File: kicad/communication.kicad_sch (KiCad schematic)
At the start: 24 parts, among them J1 Screw_Terminal_01x03, J2 Screw_Terminal_01x03, J3 Conn_ARM_SWD_TagConnect_TC203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, P1 GT-USB-7014F

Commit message: [simulations] Added debouncing, added RC circuit, cleaned up LC-ladder, [scripts] (filtering) added usb-section, started working on debouncing equations, [kicad] Additional CAN configuration added, filtering capacitor added for USB-power section
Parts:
- added C30: 1uF, symbol Device:C_Small
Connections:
- net GND: now also C30.2
- net USB_VBUS: now also C30.1
- no-connect marks 12 -> 13
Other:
- note added: "Add 1 uF capacitor for filtering (pole: 1/(1e-6) > 1 MHz)"
- note added: "TXD, NSIL, STBY internally pulled-up STBY: pulled down to enable normal-mode"
- moved on the sheet: R36
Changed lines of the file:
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@@
   (junction (at 172.72 30.48) (diameter 0) (color 0 0 0 0)
   )
+  (junction (at 58.42 173.355) (diameter 0) (color 0 0 0 0)
+  )
   (junction (at 152.4 46.99) (diameter 0) (color 0 0 0 0)
   )
@@
   )
   (junction (at 168.91 30.48) (diameter 0) (color 0 0 0 0)
-  )
-  (junction (at 58.42 170.18) (diameter 0) (color 0 0 0 0)
   )
   (junction (at 72.39 54.61) (diameter 0) (color 0 0 0 0)
@@
   (no_connect (at 91.44 109.22))
   (no_connect (at 91.44 124.46))
+  (no_connect (at 53.34 48.26))
   (no_connect (at 91.44 127))
   (no_connect (at 91.44 132.08))
@@
   (no_connect (at 91.44 104.14))
   (no_connect (at 91.44 134.62))
+  (wire (pts (xy 48.895 44.45) (xy 53.34 44.45))
+    (stroke (width 0) (type default))
+  )
   (wire (pts (xy 163.83 77.47) (xy 163.83 86.36))
     (stroke (width 0) (type default))
@@
     (stroke (width 0) (type default))
   )
+  (wire (pts (xy 43.18 166.37) (xy 43.18 165.1))
+    (stroke (width 0) (type default))
+  )
   (wire (pts (xy 168.91 41.91) (xy 176.53 41.91))
     (stroke (width 0) (type default))
@@
     (stroke (width 0) (type default))
   )
+  (wire (pts (xy 58.42 174.625) (xy 58.42 173.355))
+    (stroke (width 0) (type default))
+  )
   (wire (pts (xy 91.44 160.02) (xy 58.42 160.02))
     (stroke (width 0) (type default))
   )
-  (wire (pts (xy 52.07 170.18) (xy 58.42 170.18))
+  (wire (pts (xy 55.245 173.355) (xy 58.42 173.355))
     (stroke (width 0) (type default))
   )
@@
     (stroke (width 0) (type default))
   )
+  (wire (pts (xy 58.42 167.64) (xy 58.42 173.355))
+    (stroke (width 0) (type default))
+  )
   (wire (pts (xy 172.72 38.1) (xy 172.72 39.37))
     (stroke (width 0) (type default))
@@
     (stroke (width 0) (type default))
   )
+  (wire (pts (xy 58.42 180.34) (xy 58.42 179.705))
+    (stroke (width 0) (type default))
+  )
   (wire (pts (xy 72.39 49.53) (xy 77.47 49.53))
     (stroke (width 0) (type default))
@@
     (stroke (width 0) (type default))
   )
-  (wire (pts (xy 58.42 177.8) (xy 58.42 179.07))
-    (stroke (width 0) (type default))
-  )
   (wire (pts (xy 72.39 54.61) (xy 72.39 49.53))
     (stroke (width 0) (type default))
@@
     (stroke (width 0) (type default))
   )
-  (wire (pts (xy 58.42 167.64) (xy 58.42 170.18))
-    (stroke (width 0) (type default))
-  )
   (wire (pts (xy 93.98 46.99) (xy 90.17 46.99))
     (stroke (width 0) (type default))
@@
     (stroke (width 0) (type default))
   )
-  (wire (pts (xy 58.42 170.18) (xy 58.42 172.72))
-    (stroke (width 0) (type default))
-  )
   (wire (pts (xy 106.68 93.98) (xy 114.3 93.98))
     (stroke (width 0) (type default))
@@
   )
   (wire (pts (xy 157.48 83.82) (xy 168.91 83.82))
+    (stroke (width 0) (type default))
+  )
+  (wire (pts (xy 43.18 161.29) (xy 43.18 160.02))
     (stroke (width 0) (type default))
   )
@@
     (effects (font (size 1.27 1.27)) (justify left bottom))
   )
+  (text "Add 1 uF capacitor for filtering (pole: 1/(1e-6) > 1 MHz)"
+    (at 43.18 194.945 0)
+    (effects (font (size 1.27 1.27)) (justify left bottom))
+  )
+  (text "TXD, NSIL, STBY internally pulled-up\nSTBY: pulled down to enable normal-mode"
+    (at 27.94 78.105 0)
+    (effects (font (size 1.27 1.27)) (justify left bottom))
+  )
   (text "Pull-up resistors chosen at random\nwon't work for high bus-capacitance + speed"
     (at 138.43 95.25 0)
@@
     )
   )
-  (global_label "USB_SENSE" (shape input) (at 52.07 170.18 180) (fields_autoplaced)
+  (global_label "USB_SENSE" (shape input) (at 55.245 173.355 180) (fields_autoplaced)
     (effects (font (size 1.27 1.27)) (justify right))
-    (property "Intersheetrefs" "${INTERSHEET_REFS}" (at 38.2597 170.18 0)
+    (property "Intersheetrefs" "${INTERSHEET_REFS}" (at 41.4347 173.355 0)
       (effects (font (size 1.27 1.27)) (justify right) hide)
     )
@@
     )
   )
-  (symbol (lib_id "power:GND") (at 58.42 179.07 0) (unit 1)
-    (in_bom yes) (on_board yes) (dnp no) (fields_autoplaced)
-    (property "Reference" "#PWR031" (at 58.42 185.42 0)
-      (effects (font (size 1.27 1.27)) hide)
-    )
-    (property "Value" "GND" (at 58.42 184.15 0)
-      (effects (font (size 1.27 1.27)))
-    )
-    (property "Footprint" "" (at 58.42 179.07 0)
-      (effects (font (size 1.27 1.27)) hide)
-    )
-    (property "Datasheet" "" (at 58.42 179.07 0)
+  (symbol (lib_id "power:GND") (at 58.42 180.34 0) (unit 1)
+    (in_bom yes) (on_board yes) (dnp no) (fields_autoplaced)
+    (property "Reference" "#PWR031" (at 58.42 186.69 0)
+      (effects (font (size 1.27 1.27)) hide)
+    )
+    (property "Value" "GND" (at 58.42 185.42 0)
+      (effects (font (size 1.27 1.27)))
+    )
+    (property "Footprint" "" (at 58.42 180.34 0)
+      (effects (font (size 1.27 1.27)) hide)
+    )
+    (property "Datasheet" "" (at 58.42 180.34 0)
       (effects (font (size 1.27 1.27)) hide)
     )
@@
     )
   )
-  (symbol (lib_id "Device:R_Small") (at 58.42 175.26 0) (unit 1)
-    (in_bom yes) (on_board yes) (dnp no) (fields_autoplaced)
-    (property "Reference" "R36" (at 60.96 173.99 0)
-      (effects (font (size 1.27 1.27)) (justify left))
-    )
-    (property "Value" "21k" (at 60.96 176.53 0)
-      (effects (font (size 1.27 1.27)) (justify left))
-    )
-    (property "Footprint" "" (at 58.42 175.26 0)
-      (effects (font (size 1.27 1.27)) hide)
-    )
-    (property "Datasheet" "~" (at 58.42 175.26 0)
+  (symbol (lib_id "Device:R_Small") (at 58.42 177.165 0) (unit 1)
+    (in_bom yes) (on_board yes) (dnp no) (fields_autoplaced)
+    (property "Reference" "R36" (at 60.96 175.895 0)
+      (effects (font (size 1.27 1.27)) (justify left))
+    )
+    (property "Value" "21k" (at 60.96 178.435 0)
+      (effects (font (size 1.27 1.27)) (justify left))
+    )
+    (property "Footprint" "" (at 58.42 177.165 0)
+      (effects (font (size 1.27 1.27)) hide)
+    )
+    (property "Datasheet" "~" (at 58.42 177.165 0)
       (effects (font (size 1.27 1.27)) hide)
     )
@@
         (path "/91e2f46a-700b-4d7a-a06a-22469f63223f/53dc30ee-9af6-4771-8676-c78726df5d90"
           (reference "R36") (unit 1)
+        )
+      )
+    )
+  )
+  (symbol (lib_id "power:GND") (at 48.895 44.45 0) (unit 1)
+    (in_bom yes) (on_board yes) (dnp no) (fields_autoplaced)
+    (property "Reference" "#PWR059" (at 48.895 50.8 0)
+      (effects (font (size 1.27 1.27)) hide)
+    )
+    (property "Value" "GND" (at 48.895 49.53 0)
+      (effects (font (size 1.27 1.27)))
+    )
+    (property "Footprint" "" (at 48.895 44.45 0)
+      (effects (font (size 1.27 1.27)) hide)
+    )
+    (property "Datasheet" "" (at 48.895 44.45 0)
+      (effects (font (size 1.27 1.27)) hide)
+    )
+    (pin "1")
+    (instances
+      (project "bldc_project"
+        (path "/91e2f46a-700b-4d7a-a06a-22469f63223f/53dc30ee-9af6-4771-8676-c78726df5d90"
+          (reference "#PWR059") (unit 1)
         )
       )
@@
     )
   )
+  (symbol (lib_id "Device:C_Small") (at 43.18 163.83 0) (unit 1)
+    (in_bom yes) (on_board yes) (dnp no) (fields_autoplaced)
+    (property "Reference" "C30" (at 45.72 162.5663 0)
+      (effects (font (size 1.27 1.27)) (justify left))
+    )
+    (property "Value" "1uF" (at 45.72 165.1063 0)
+      (effects (font (size 1.27 1.27)) (justify left))
+    )
+    (property "Footprint" "" (at 43.18 163.83 0)
+      (effects (font (size 1.27 1.27)) hide)
+    )
+    (property "Datasheet" "~" (at 43.18 163.83 0)
+      (effects (font (size 1.27 1.27)) hide)
+    )
+    (pin "2")
+    (pin "1")
+    (instances
+      (project "bldc_project"
+        (path "/91e2f46a-700b-4d7a-a06a-22469f63223f/53dc30ee-9af6-4771-8676-c78726df5d90"
+          (reference "C30") (unit 1)
+        )
+      )
+    )
+  )
   (symbol (lib_id "Diode:SMAJ13A") (at 172.72 34.29 90) (unit 1)
     (in_bom yes) (on_board yes) (dnp no)
@@
         )
       )
+    )
+  )
+  (symbol (lib_id "power:GND") (at 43.18 165.1 0) (unit 1)
+    (in_bom yes) (on_board yes) (dnp no) (fields_autoplaced)
+    (property "Reference" "#PWR058" (at 43.18 171.45 0)
+      (effects (font (size 1.27 1.27)) hide)
+    )
+    (property "Value" "GND" (at 43.18 170.18 0)
+      (effects (font (size 1.27 1.27)))
+    )
+    (property "Footprint" "" (at 43.18 165.1 0)
+      (effects (font (size 1.27 1.27)) hide)
+    )
+    (property "Datasheet" "" (at 43.18 165.1 0)
+      (effects (font (size 1.27 1.27)) hide)
+    )
+    (pin "1")
+    (instances
+      (project "bldc_project"
+        (path "/91e2f46a-700b-4d7a-a06a-22469f63223f/53dc30ee-9af6-4771-8676-c78726df5d90"
+          (reference "#PWR058") (unit 1)
+        )
+      )

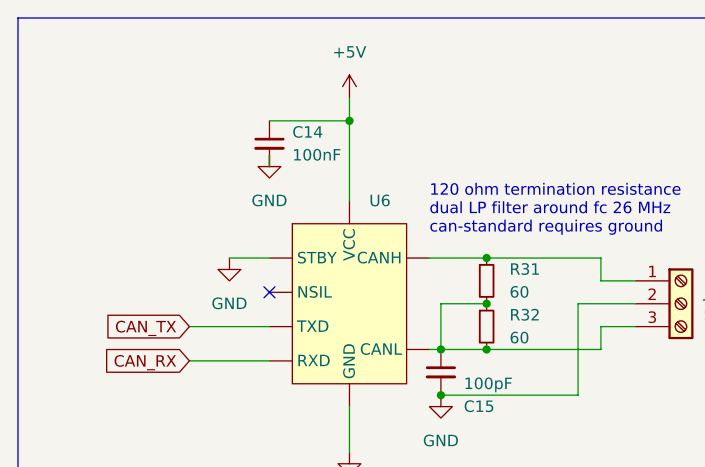
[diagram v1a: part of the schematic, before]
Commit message: [kicad] added component numbers from jlcpcb [scripts] added bulk capacitor plot
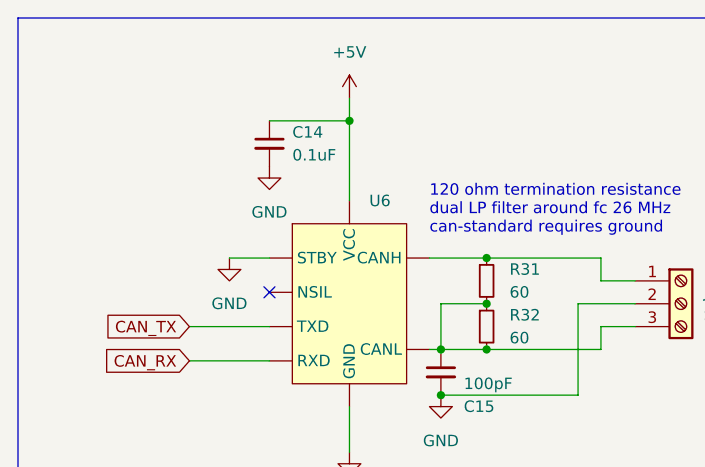
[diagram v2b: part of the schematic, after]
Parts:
- C14: value 100nF -> 0.1uF; footprint (none) -> Resistor_SMD:R_0402_1005Metric; jlcpcb (none) -> C307331
- C16: footprint (none) -> Resistor_SMD:R_0402_1005Metric; jlcpcb (none) -> C307331
- C30: footprint (none) -> Capacitor_SMD:C_1206_3216Metric; MFR.Part (none) -> CL31B105KBHNNNE; jlpcb (none) -> C1848
- J1, J2: footprint (none) -> TerminalBlock:TerminalBlock_bornier-3_P5.08mm; jlcpcb (none) -> C72334
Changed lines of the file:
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@@
-    (stroke (width 0) (type default))
-  )
-  (wire (pts (xy 53.34 33.02) (xy 53.34 34.29))
     (stroke (width 0) (type default))
   )
@@
     )
   )
+  (symbol (lib_id "Device:C_Small") (at 152.4 50.8 0) (unit 1)
+    (in_bom yes) (on_board yes) (dnp no) (fields_autoplaced)
+    (property "Reference" "C16" (at 154.94 49.5363 0)
+      (effects (font (size 1.27 1.27)) (justify left))
+    )
+    (property "Value" "0.1uF" (at 154.94 52.0763 0)
+      (effects (font (size 1.27 1.27)) (justify left))
+    )
+    (property "Footprint" "Resistor_SMD:R_0402_1005Metric" (at 152.4 50.8 0)
+      (effects (font (size 1.27 1.27)) hide)
+    )
+    (property "Datasheet" "https://wmsc.lcsc.com/wmsc/upload/file/pdf/v2/lcsc/2304140030_Samsung-Electro-Mechanics-CL05B104KB54PNC_C307331.pdf" (at 152.4 50.8 0)
+      (effects (font (size 1.27 1.27)) hide)
+    )
+    (property "jlcpcb" "C307331" (at 152.4 50.8 0)
+      (effects (font (size 1.27 1.27)) hide)
+    )
+    (pin "1")
+    (pin "2")
+    (instances
+      (project "bldc_project"
+        (path "/91e2f46a-700b-4d7a-a06a-22469f63223f/53dc30ee-9af6-4771-8676-c78726df5d90"
+          (reference "C16") (unit 1)
+        )
+      )
+    )
+  )
   (symbol (lib_id "power:+3.3V") (at 186.69 52.07 180) (unit 1)
     (in_bom yes) (on_board yes) (dnp no) (fields_autoplaced)
@@
         (path "/91e2f46a-700b-4d7a-a06a-22469f63223f/53dc30ee-9af6-4771-8676-c78726df5d90"
           (reference "#PWR036") (unit 1)
+        )
+      )
+    )
+  )
+  (symbol (lib_id "Device:C_Small") (at 53.34 31.75 0) (unit 1)
+    (in_bom yes) (on_board yes) (dnp no) (fields_autoplaced)
+    (property "Reference" "C14" (at 55.88 30.4863 0)
+      (effects (font (size 1.27 1.27)) (justify left))
+    )
+    (property "Value" "0.1uF" (at 55.88 33.0263 0)
+      (effects (font (size 1.27 1.27)) (justify left))
+    )
+    (property "Footprint" "Resistor_SMD:R_0402_1005Metric" (at 53.34 31.75 0)
+      (effects (font (size 1.27 1.27)) hide)
+    )
+    (property "Datasheet" "https://wmsc.lcsc.com/wmsc/upload/file/pdf/v2/lcsc/2304140030_Samsung-Electro-Mechanics-CL05B104KB54PNC_C307331.pdf" (at 53.34 31.75 0)
+      (effects (font (size 1.27 1.27)) hide)
+    )
+    (property "jlcpcb" "C307331" (at 53.34 31.75 0)
+      (effects (font (size 1.27 1.27)) hide)
+    )
+    (pin "1")
+    (pin "2")
+    (instances
+      (project "bldc_project"
+        (path "/91e2f46a-700b-4d7a-a06a-22469f63223f/53dc30ee-9af6-4771-8676-c78726df5d90"
+          (reference "C14") (unit 1)
         )
       )
@@
     )
   )
-  (symbol (lib_id "Connector:Screw_Terminal_01x03") (at 173.99 86.36 0) (unit 1)
-    (in_bom yes) (on_board yes) (dnp no) (fields_autoplaced)
-    (property "Reference" "J1" (at 176.53 85.09 0)
-      (effects (font (size 1.27 1.27)) (justify left))
-    )
-    (property "Value" "Screw_Terminal_01x03" (at 176.53 87.63 0)
-      (effects (font (size 1.27 1.27)) (justify left))
-    )
-    (property "Footprint" "" (at 173.99 86.36 0)
-      (effects (font (size 1.27 1.27)) hide)
-    )
-    (property "Datasheet" "~" (at 173.99 86.36 0)
-      (effects (font (size 1.27 1.27)) hide)
-    )
-    (pin "1")
-    (pin "2")
-    (pin "3")
-    (instances
-      (project "bldc_project"
-        (path "/91e2f46a-700b-4d7a-a06a-22469f63223f/53dc30ee-9af6-4771-8676-c78726df5d90"
-          (reference "J1") (unit 1)
-        )
-      )
-    )
-  )
   (symbol (lib_id "power:+3.3V") (at 157.48 72.39 0) (unit 1)
     (in_bom yes) (on_board yes) (dnp no) (fields_autoplaced)
@@
     )
   )
+  (symbol (lib_id "Connector:Screw_Terminal_01x03") (at 173.99 86.36 0) (unit 1)
+    (in_bom yes) (on_board yes) (dnp no) (fields_autoplaced)
+    (property "Reference" "J1" (at 176.53 85.09 0)
+      (effects (font (size 1.27 1.27)) (justify left))
+    )
+    (property "Value" "Screw_Terminal_01x03" (at 176.53 87.63 0)
+      (effects (font (size 1.27 1.27)) (justify left))
+    )
+    (property "Footprint" "TerminalBlock:TerminalBlock_bornier-3_P5.08mm" (at 173.99 86.36 0)
+      (effects (font (size 1.27 1.27)) hide)
+    )
+    (property "Datasheet" "https://wmsc.lcsc.com/wmsc/upload/file/pdf/v2/lcsc/1912251709_Ningbo-Kangnex-Elec-WJ500V-5-08-3P_C72334.pdf" (at 173.99 86.36 0)
+      (effects (font (size 1.27 1.27)) hide)
+    )
+    (property "jlcpcb" "C72334" (at 173.99 86.36 0)
+      (effects (font (size 1.27 1.27)) hide)
+    )
+    (pin "1")
+    (pin "2")
+    (pin "3")
+    (instances
+      (project "bldc_project"
+        (path "/91e2f46a-700b-4d7a-a06a-22469f63223f/53dc30ee-9af6-4771-8676-c78726df5d90"
+          (reference "J1") (unit 1)
+        )
+      )
+    )
+  )
   (symbol (lib_id "Diode:SMAJ13A") (at 165.1 34.29 90) (unit 1)
     (in_bom yes) (on_board yes) (dnp no)
@@
     )
   )
-  (symbol (lib_id "Device:C_Small") (at 53.34 31.75 0) (unit 1)
-    (in_bom yes) (on_board yes) (dnp no) (fields_autoplaced)
-    (property "Reference" "C14" (at 55.88 30.4863 0)
-      (effects (font (size 1.27 1.27)) (justify left))
-    )
-    (property "Value" "100nF" (at 55.88 33.0263 0)
-      (effects (font (size 1.27 1.27)) (justify left))
-    )
-    (property "Footprint" "" (at 53.34 31.75 0)
-      (effects (font (size 1.27 1.27)) hide)
-    )
-    (property "Datasheet" "~" (at 53.34 31.75 0)
-      (effects (font (size 1.27 1.27)) hide)
-    )
-    (pin "1")
-    (pin "2")
-    (instances
-      (project "bldc_project"
-        (path "/91e2f46a-700b-4d7a-a06a-22469f63223f/53dc30ee-9af6-4771-8676-c78726df5d90"
-          (reference "C14") (unit 1)
-        )
-      )
-    )
-  )
   (symbol (lib_id "Device:R_Small") (at 82.55 165.1 180) (unit 1)
     (in_bom yes) (on_board yes) (dnp no) (fields_autoplaced)
@@
     )
   )
-  (symbol (lib_id "power:GND") (at 53.34 33.02 0) (unit 1)
-    (in_bom yes) (on_board yes) (dnp no) (fields_autoplaced)
-    (property "Reference" "#PWR026" (at 53.34 39.37 0)
-      (effects (font (size 1.27 1.27)) hide)
-    )
-    (property "Value" "GND" (at 53.34 38.1 0)
-      (effects (font (size 1.27 1.27)))
-    )
-    (property "Footprint" "" (at 53.34 33.02 0)
-      (effects (font (size 1.27 1.27)) hide)
-    )
-    (property "Datasheet" "" (at 53.34 33.02 0)
+  (symbol (lib_id "power:GND") (at 53.34 34.29 0) (unit 1)
+    (in_bom yes) (on_board yes) (dnp no) (fields_autoplaced)
+    (property "Reference" "#PWR026" (at 53.34 40.64 0)
+      (effects (font (size 1.27 1.27)) hide)
+    )
+    (property "Value" "GND" (at 53.34 39.37 0)
+      (effects (font (size 1.27 1.27)))
+    )
+    (property "Footprint" "" (at 53.34 34.29 0)
+      (effects (font (size 1.27 1.27)) hide)
+    )
+    (property "Datasheet" "" (at 53.34 34.29 0)
       (effects (font (size 1.27 1.27)) hide)
     )
@@
       (effects (font (size 1.27 1.27)) (justify left))
     )
-    (property "Footprint" "" (at 99.06 49.53 0)
-      (effects (font (size 1.27 1.27)) hide)
-    )
-    (property "Datasheet" "~" (at 99.06 49.53 0)
+    (property "Footprint" "TerminalBlock:TerminalBlock_bornier-3_P5.08mm" (at 99.06 49.53 0)
+      (effects (font (size 1.27 1.27)) hide)
+    )
+    (property "Datasheet" "https://wmsc.lcsc.com/wmsc/upload/file/pdf/v2/lcsc/1912251709_Ningbo-Kangnex-Elec-WJ500V-5-08-3P_C72334.pdf" (at 99.06 49.53 0)
+      (effects (font (size 1.27 1.27)) hide)
+    )
+    (property "jlcpcb" "C72334" (at 99.06 49.53 0)
       (effects (font (size 1.27 1.27)) hide)
     )
@@
       (effects (font (size 1.27 1.27)) (justify left))
     )
-    (property "Footprint" "" (at 43.18 163.83 0)
-      (effects (font (size 1.27 1.27)) hide)
-    )
-    (property "Datasheet" "~" (at 43.18 163.83 0)
+    (property "Footprint" "Capacitor_SMD:C_1206_3216Metric" (at 43.18 163.83 0)
+      (effects (font (size 1.27 1.27)) hide)
+    )
+    (property "Datasheet" "https://wmsc.lcsc.com/wmsc/upload/file/pdf/v2/lcsc/2304140030_Samsung-Electro-Mechanics-CL31B105KBHNNNE_C1848.pdf" (at 43.18 163.83 0)
+      (effects (font (size 1.27 1.27)) hide)
+    )
+    (property "jlpcb" "C1848" (at 43.18 163.83 0)
+      (effects (font (size 1.27 1.27)) hide)
+    )
+    (property "MFR.Part" "CL31B105KBHNNNE" (at 43.18 163.83 0)
       (effects (font (size 1.27 1.27)) hide)
     )
@@
         )
       )
-    )
-  )
-  (symbol (lib_id "Device:C_Small") (at 152.4 50.8 0) (unit 1)
-    (in_bom yes) (on_board yes) (dnp no) (fields_autoplaced)
-    (property "Reference" "C16" (at 154.94 49.5363 0)
-      (effects (font (size 1.27 1.27)) (justify left))
-    )
-    (property "Value" "0.1uF" (at 154.94 52.0763 0)
-      (effects (font (size 1.27 1.27)) (justify left))
-    )
-    (property "Footprint" "" (at 152.4 50.8 0)
-      (effects (font (size 1.27 1.27)) hide)
-    )
-    (property "Datasheet" "~" (at 152.4 50.8 0)
-      (effects (font (size 1.27 1.27)) hide)
-    )
-    (pin "2")
-    (pin "1")
-    (instances
-      (project "bldc_project"
-        (path "/91e2f46a-700b-4d7a-a06a-22469f63223f/53dc30ee-9af6-4771-8676-c78726df5d90"
-          (reference "C16") (unit 1)
-        )
-      )
